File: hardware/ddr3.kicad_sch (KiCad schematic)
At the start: 4 parts, among them U2 H5TQ4G63EFR, U3 H5TQ4G63EFR

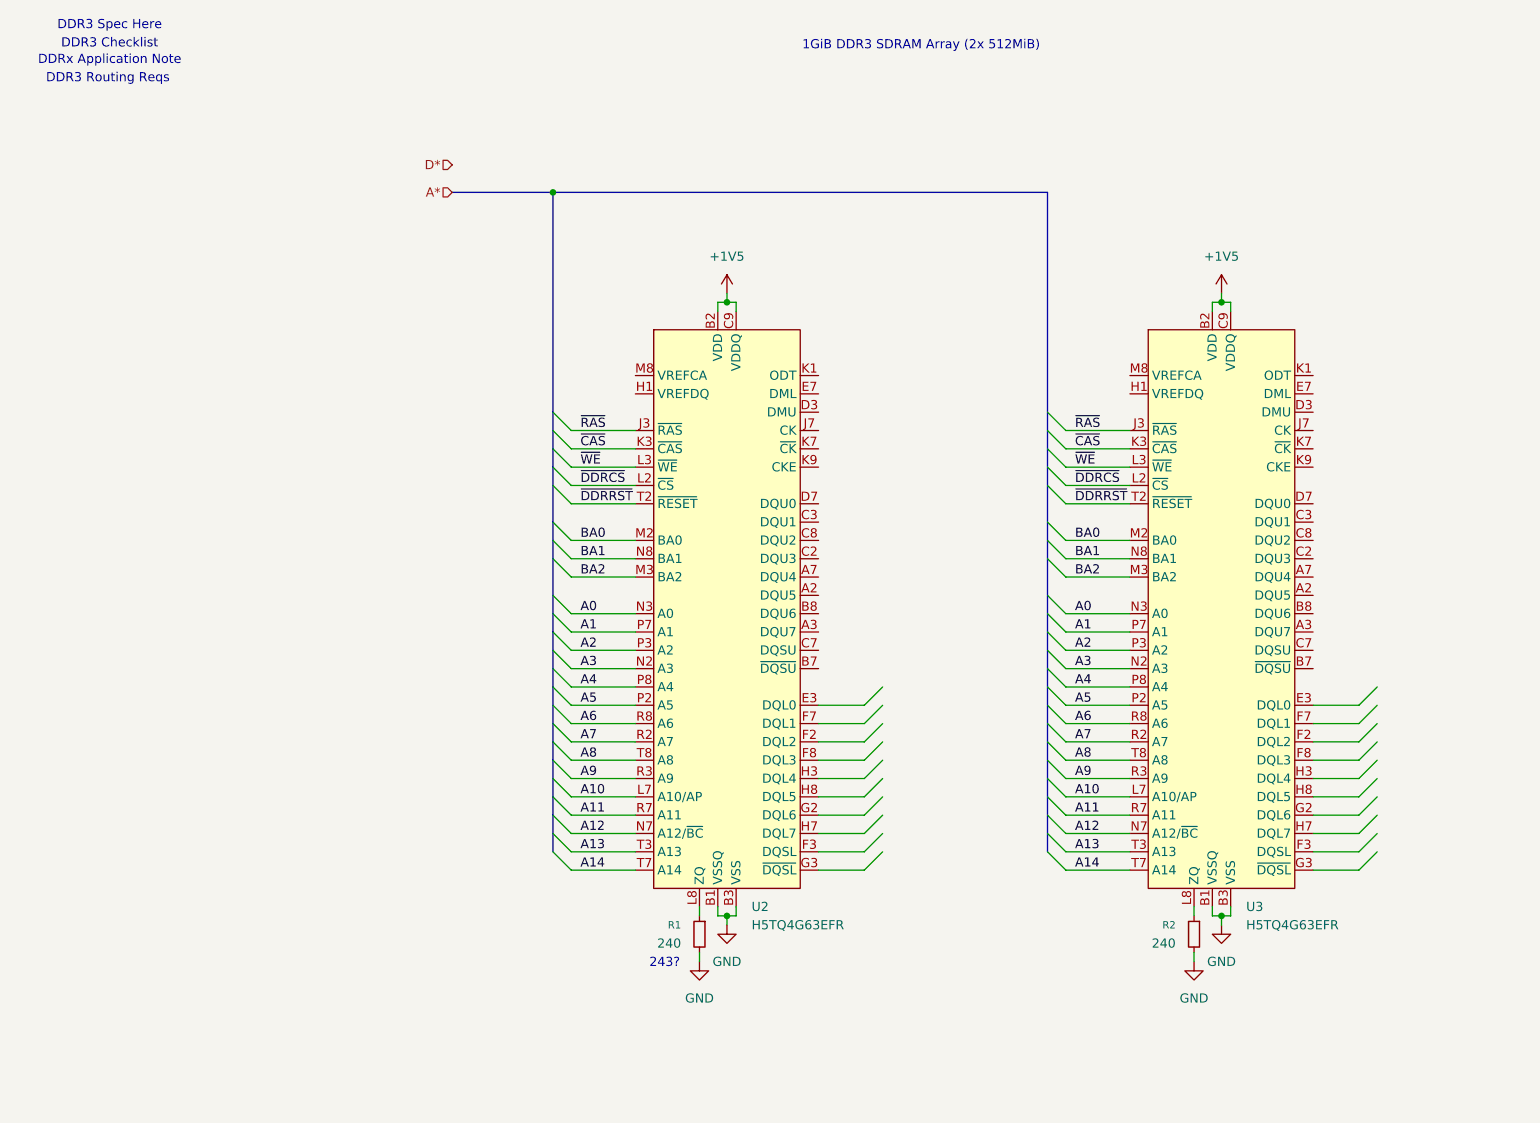
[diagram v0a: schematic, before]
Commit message: DDR3 schematic made
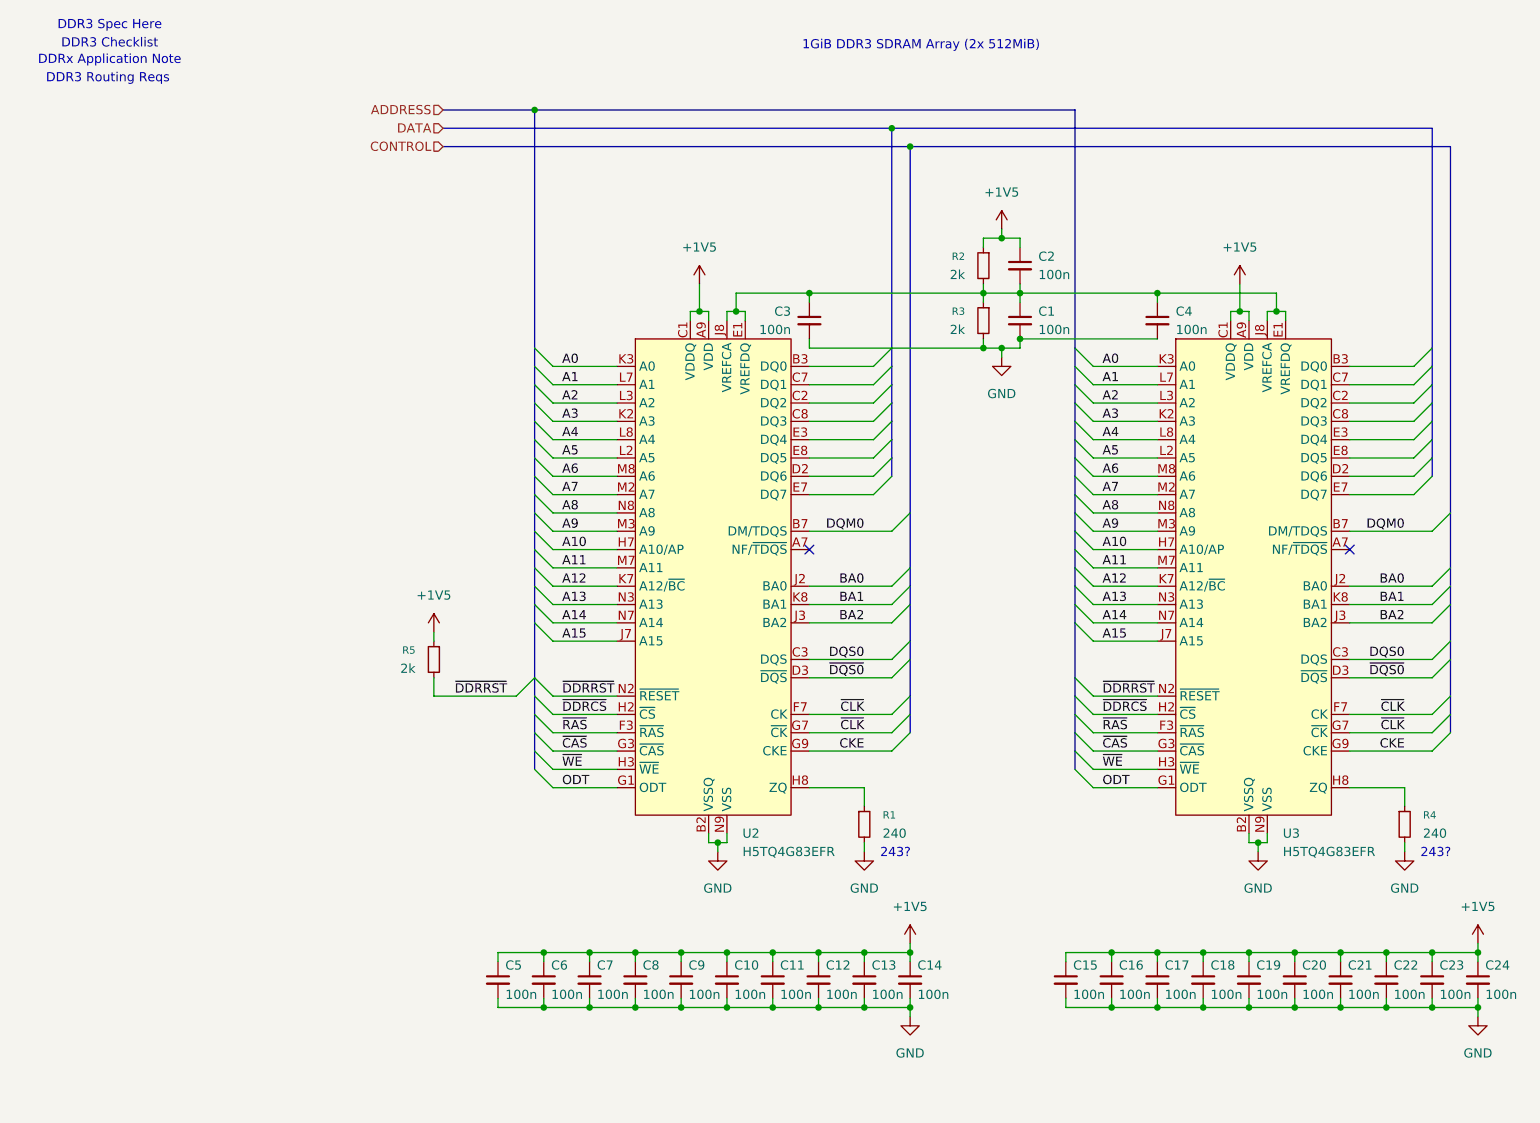
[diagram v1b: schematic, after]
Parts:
- removed U2, U3: H5TQ4G63EFR, Package_BGA:FBGA-96_7.5x13mm_Layout9x16_P0.8mm, symbol slate-lib:H5TQ4G63EFR
- added C1, C10, C11, C12, C13, C14, C15, C16, C17, C18, C19, C2, C20, C21, C22, C23, C24, C3, C4, C5, C6, C7, C8, C9: 100n, Capacitor_SMD:C_0201_0603Metric, symbol Device:C_Small
- added R3, R5: 2k, Resistor_SMD:R_0201_0603Metric, symbol Device:R_Small
- added R4: 240, Resistor_SMD:R_0201_0603Metric, symbol Device:R_Small
- added U2, U3: H5TQ4G83EFR, Package_BGA:FBGA-78_7.5x11mm_Layout2x3x13_P0.8mm, symbol slate-lib:H5TQ4G83EFR
- R2: value 240 -> 2k
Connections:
- net +1V5: now also R2.1, C10.1, C11.1, C12.1, C13.1, C14.1, C15.1, C16.1, C17.1, C18.1, C19.1, C2.1, C20.1, C21.1, C22.1, C23.1, C24.1, C5.1, C6.1, C7.1, C8.1, C9.1, R5.1, U2.A2 (VDD), U2.A9 (VDD), U2.B9 (VDDQ), U2.C1 (VDDQ), U2.D7 (VDD), U2.E2 (VDDQ), U2.E9 (VDDQ), U2.G2 (VDD), U2.G8 (VDD), U2.K1 (VDD), U2.K9 (VDD), U2.M1 (VDD), U2.M9 (VDD), U3.A2 (VDD), U3.A9 (VDD), U3.B9 (VDDQ), U3.C1 (VDDQ), U3.D7 (VDD), U3.E2 (VDDQ), U3.E9 (VDDQ), U3.G2 (VDD), U3.G8 (VDD), U3.K1 (VDD), U3.K9 (VDD), U3.M1 (VDD), U3.M9 (VDD)
- net A0: now also U2.K3 (A0), U3.K3 (A0)
- net A1: now also U2.L7 (A1), U3.L7 (A1)
- net A10: now also U2.H7 (A10/AP), U3.H7 (A10/AP)
- net A11: now also U2.M7 (A11), U3.M7 (A11)
- net A12: now also U2.K7 (A12/~{BC}), U3.K7 (A12/~{BC})
- net A13: now also U2.N3 (A13), U3.N3 (A13)
- net A14: now also U2.N7 (A14), U3.N7 (A14)
- net A2: now also U2.L3 (A2), U3.L3 (A2)
- net A3: now also U2.K2 (A3), U3.K2 (A3)
- net A4: now also U2.L8 (A4), U3.L8 (A4)
- net A5: now also U2.L2 (A5), U3.L2 (A5)
- net A6: now also U2.M8 (A6), U3.M8 (A6)
- net A7: now also U2.M2 (A7), U3.M2 (A7)
- net A8: now also U2.N8 (A8), U3.N8 (A8)
- net A9: now also U2.M3 (A9), U3.M3 (A9)
- net BA0: now also U2.J2 (BA0), U3.J2 (BA0)
- net BA1: now also U2.K8 (BA1), U3.K8 (BA1)
- net BA2: now also U2.J3 (BA2), U3.J3 (BA2)
- net GND: now also C1.2, C10.2, C11.2, C12.2, C13.2, C14.2, C15.2, C16.2, C17.2, C18.2, C19.2, C20.2, C21.2, C22.2, C23.2, C24.2, C3.2, C4.2, C5.2, C6.2, C7.2, C8.2, C9.2, R3.2, R4.2, U2.A1 (VSS), U2.A8 (VSS), U2.B1 (VSS), U2.B2 (VSSQ), U2.B8 (VSSQ), U2.C9 (VSSQ), U2.D1 (VSSQ), U2.D8 (VSS), U2.D9 (VSSQ), U2.F2 (VSS), U2.F8 (VSS), U2.J1 (VSS), U2.J9 (VSS), U2.L1 (VSS), U2.L9 (VSS), U2.N1 (VSS), U2.N9 (VSS), U3.A1 (VSS), U3.A8 (VSS), U3.B1 (VSS), U3.B2 (VSSQ), U3.B8 (VSSQ), U3.C9 (VSSQ), U3.D1 (VSSQ), U3.D8 (VSS), U3.D9 (VSSQ), U3.F2 (VSS), U3.F8 (VSS), U3.J1 (VSS), U3.J9 (VSS), U3.L1 (VSS), U3.L9 (VSS), U3.N1 (VSS), U3.N9 (VSS); no longer R2.2
- net ~{CAS}: now also U2.G3 (~{CAS}), U3.G3 (~{CAS})
- net ~{DDRCS}: now also U2.H2 (~{CS}), U3.H2 (~{CS})
- net ~{DDRRST}: now also R5.2, U2.N2 (~{RESET}), U3.N2 (~{RESET})
- net ~{RAS}: now also U2.F3 (~{RAS}), U3.F3 (~{RAS})
- net ~{WE}: now also U2.H3 (~{WE}), U3.H3 (~{WE})
- net at R1.1: now also U2.H8 (ZQ)
- new net: C1.1, C2.2, C3.1, C4.1, R2.2, R3.1, U2.E1 (VREFDQ), U2.J8 (VREFCA), U3.E1 (VREFDQ), U3.J8 (VREFCA)
- new net: U3.A3 (NC), U3.F1 (NC), U3.F9 (NC), U3.H1 (NC), U3.H9 (NC)
- new net: R4.1, U3.H8 (ZQ)
- new net: U2.A3 (NC), U2.F1 (NC), U2.F9 (NC), U2.H1 (NC), U2.H9 (NC)
- new net A15: U2.J7 (A15), U3.J7 (A15)
- new net CKE: U2.G9 (CKE), U3.G9 (CKE)
- new net DQM0: U2.B7 (DM/TDQS), U3.B7 (DM/TDQS)
- new net DQS0: U2.C3 (DQS), U3.C3 (DQS)
- new net ODT: U2.G1 (ODT), U3.G1 (ODT)
- new net ~{CLK}: U2.F7 (CK), U2.G7 (~{CK}), U3.F7 (CK), U3.G7 (~{CK})
- new net ~{DQS0}: U2.D3 (~{DQS}), U3.D3 (~{DQS})
- no-connect marks 0 -> 2
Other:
- moved on the sheet: R1

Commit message: Update
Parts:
- added R7, R8: 240, Resistor_SMD:R_0201_0603Metric, symbol Device:R_Small
- R2, R3: value 2k -> 1k
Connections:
- net DQM0: no longer U3.B7 (DM/TDQS)
- net GND: now also R7.2, R8.2
- net CKE renamed CKE0
- net DQS0 renamed DQS0+
- net DQS0+: no longer U3.C3 (DQS)
- net ODT renamed ODT0
- net ~{CLK} renamed CLK+
- net CLK+: no longer U2.G7 (~{CK}), U3.G7 (~{CK})
- net ~{DDRCS} renamed ~{CS0}
- net ~{DDRRST} renamed ~{RESET}
- net ~{DQS0} renamed DQS0-
- net DQS0-: no longer U3.D3 (~{DQS})
- new net: R8.1, U3.H9 (ZQ1/NC)
- new net: R7.1, U2.H9 (ZQ1/NC)
- new net CKE1: U2.F9 (CKE1/NC), U3.F9 (CKE1/NC)
- new net CLK-: U2.G7 (~{CK}), U3.G7 (~{CK})
- new net DQM1: U3.B7 (DM/TDQS)
- new net DQS1+: U3.C3 (DQS)
- new net DQS1-: U3.D3 (~{DQS})
- new net ODT1: U2.F1 (ODT1/NC), U3.F1 (ODT1/NC)
- new net ~{CS1}: U2.H1 (~{CS1}/NC), U3.H1 (~{CS1}/NC)
- now unconnected: U2.A3 (NC), U3.A3 (NC)
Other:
- note added: "Check if 1k supplies enough current"
- moved on the sheet: C1, C10, C11, C12, C13, C14, C15, C16, C17, C18, C19, C2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

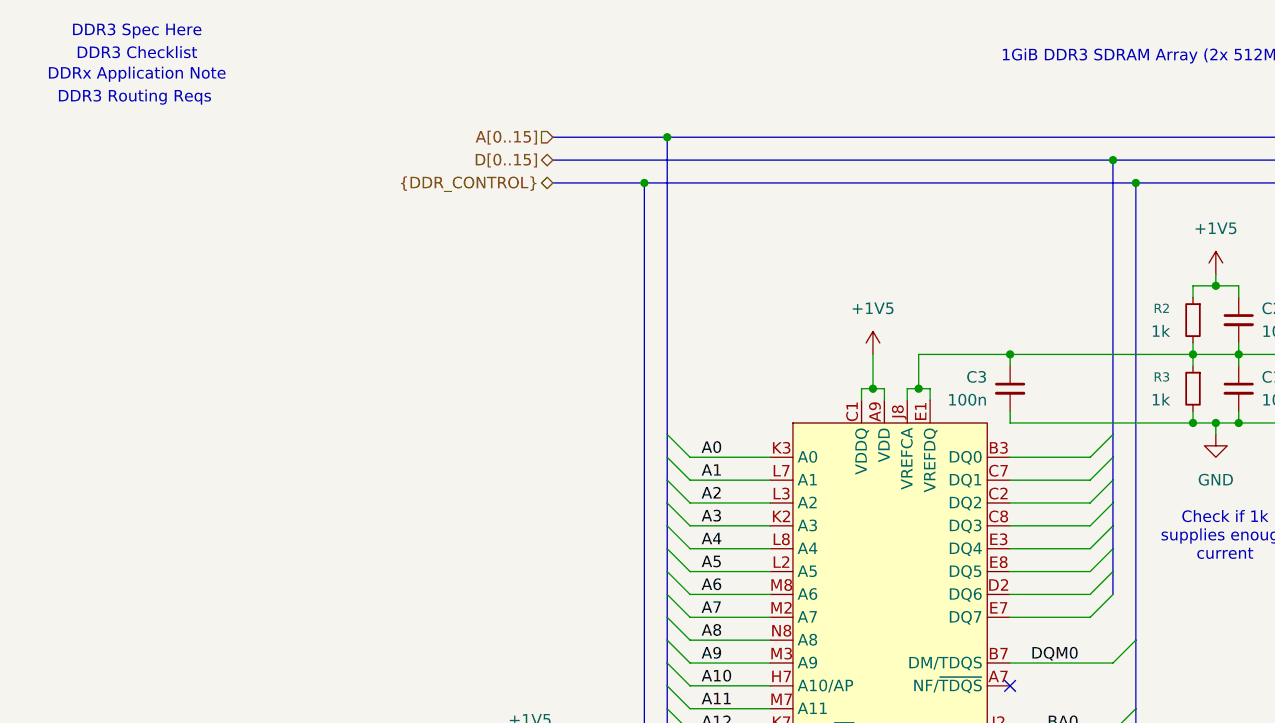
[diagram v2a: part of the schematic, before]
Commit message: Start of psu
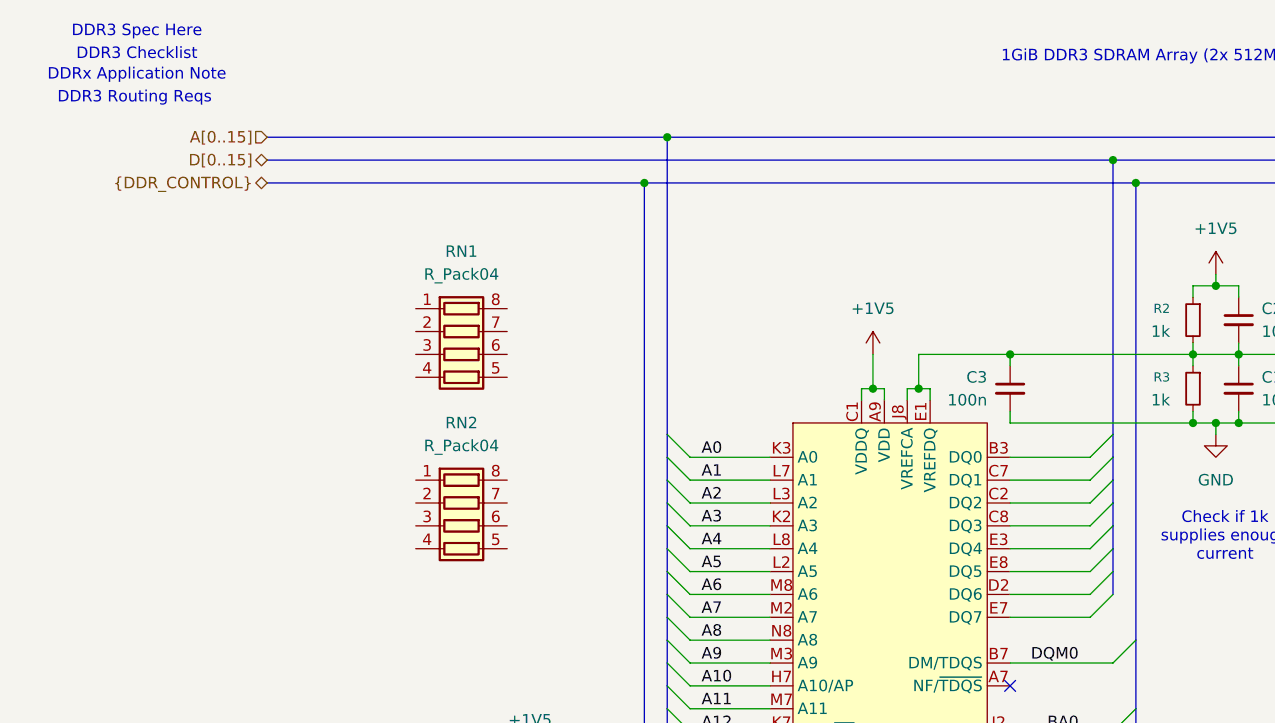
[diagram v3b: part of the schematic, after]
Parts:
- added RN1, RN2: R_Pack04, Resistor_SMD:R_Array_Concave_4x0402, symbol Device:R_Pack04
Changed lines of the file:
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@@
 	(bus
 		(pts
-			(xy 71.12 31.75) (xy 81.28 31.75)
+			(xy 39.37 31.75) (xy 81.28 31.75)
 		)
 		(stroke
@@
 	(bus
 		(pts
-			(xy 133.35 29.21) (xy 71.12 29.21)
+			(xy 133.35 29.21) (xy 39.37 29.21)
 		)
 		(stroke
@@
 	(bus
 		(pts
-			(xy 83.82 26.67) (xy 71.12 26.67)
+			(xy 83.82 26.67) (xy 39.37 26.67)
 		)
 		(stroke
@@
 	(hierarchical_label "A[0..15]"
 		(shape input)
-		(at 71.12 26.67 180)
+		(at 39.37 26.67 180)
 		(effects
 			(font
@@
 	(hierarchical_label "{DDR_CONTROL}"
 		(shape bidirectional)
-		(at 71.12 31.75 180)
+		(at 39.37 31.75 180)
 		(effects
 			(font
@@
 	(hierarchical_label "D[0..15]"
 		(shape bidirectional)
-		(at 71.12 29.21 180)
+		(at 39.37 29.21 180)
 		(effects
 			(font
@@
 	)
 	(symbol
+		(lib_id "Device:R_Pack04")
+		(at 60.96 69.85 270)
+		(unit 1)
+		(exclude_from_sim no)
+		(in_bom yes)
+		(on_board yes)
+		(dnp no)
+		(fields_autoplaced yes)
+		(property "Reference" "RN2"
+			(at 60.96 58.42 90)
+			(effects
+				(font
+					(size 1.27 1.27)
+				)
+			)
+		)
+		(property "Value" "R_Pack04"
+			(at 60.96 60.96 90)
+			(effects
+				(font
+					(size 1.27 1.27)
+				)
+			)
+		)
+		(property "Footprint" "Resistor_SMD:R_Array_Concave_4x0402"
+			(at 60.96 76.835 90)
+			(effects
+				(font
+					(size 1.27 1.27)
+				)
+				(hide yes)
+			)
+		)
+		(property "Datasheet" "~"
+			(at 60.96 69.85 0)
+			(effects
+				(font
+					(size 1.27 1.27)
+				)
+				(hide yes)
+			)
+		)
+		(property "Description" "4 resistor network, parallel topology"
+			(at 60.96 69.85 0)
+			(effects
+				(font
+					(size 1.27 1.27)
+				)
+				(hide yes)
+			)
+		)
+		(pin "8"
+		)
+		(pin "7"
+		)
+		(pin "3"
+		)
+		(pin "6"
+		)
+		(pin "1"
+		)
+		(pin "4"
+		)
+		(pin "5"
+		)
+		(pin "2"
+		)
+		(instances
+			(project "slate"
+				(path "/343587c4-adfe-4efb-aa95-3a477d6077b4/1164a079-1a3b-4be9-864c-e4cd3b379f16"
+					(reference "RN2")
+					(unit 1)
+				)
+			)
+		)
+	)
+	(symbol
 		(lib_id "Device:C_Small")
 		(at 91.44 153.67 0)
@@
 					(unit 1)
 				)
+			)
+		)
+	)
+	(symbol
+		(lib_id "Device:R_Pack04")
+		(at 60.96 50.8 270)
+		(unit 1)
+		(exclude_from_sim no)
+		(in_bom yes)
+		(on_board yes)
+		(dnp no)
+		(fields_autoplaced yes)
+		(property "Reference" "RN1"
+			(at 60.96 39.37 90)
+			(effects
+				(font
+					(size 1.27 1.27)
+				)
+			)
+		)
+		(property "Value" "R_Pack04"
+			(at 60.96 41.91 90)
+			(effects
+				(font
+					(size 1.27 1.27)
+				)
+			)
+		)
+		(property "Footprint" "Resistor_SMD:R_Array_Concave_4x0402"
+			(at 60.96 57.785 90)
+			(effects
+				(font
+					(size 1.27 1.27)
+				)
+				(hide yes)
+			)
+		)
+		(property "Datasheet" "~"
+			(at 60.96 50.8 0)
+			(effects
+				(font
+					(size 1.27 1.27)
+				)
+				(hide yes)
+			)
+		)
+		(property "Description" "4 resistor network, parallel topology"
+			(at 60.96 50.8 0)
+			(effects
+				(font
+					(size 1.27 1.27)
+				)
+				(hide yes)
+			)
+		)
+		(pin "8"
+		)
+		(pin "7"
+		)
+		(pin "3"
+		)
+		(pin "6"
+		)
+		(pin "1"
+		)
+		(pin "4"
+		)
+		(pin "5"
+		)
+		(pin "2"
+		)
+		(instances
+			(project ""
+				(path "/343587c4-adfe-4efb-aa95-3a477d6077b4/1164a079-1a3b-4be9-864c-e4cd3b379f16"
+					(reference "RN1")
+					(unit 1)
+				)
